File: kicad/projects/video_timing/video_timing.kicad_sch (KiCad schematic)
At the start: 26 parts, among them J1 peripheral_addr_bus_connector, J2 peripheral_aux_connector, J3 peripheral_membank_connector, U1 74HC161, U10 74HC30, U11 74HC30, U12 74HC30, U13 74HC30, U14 74HC30, U15 74HC30, U16 74HC30, U17 74HC30, U2 74HC161, U3 74HC161, U4 74HC161, U5 74HC161, U6 74HC04, U7 74HC04, U8 74HC00, U9 74HC00

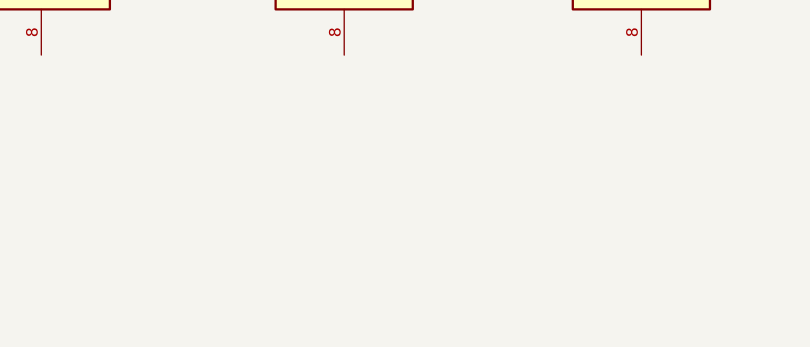
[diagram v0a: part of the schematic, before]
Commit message: Roughing out the video baords - time to switch to 157s for bank sel as well.
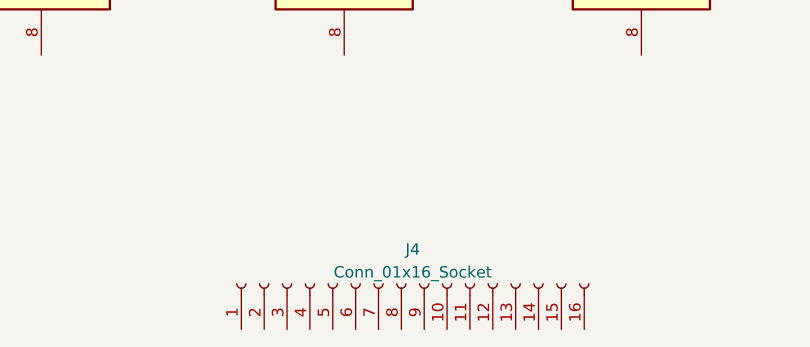
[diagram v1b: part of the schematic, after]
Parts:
- added J4: Conn_01x16_Socket, Connector_PinSocket_2.54mm:PinSocket_1x16_P2.54mm_Horizontal, symbol Connector:Conn_01x16_Socket
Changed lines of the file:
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@@
 (kicad_sch (version 20230121) (generator eeschema)
   (paper "B")
+  (bus_alias "BANK_BUS" (members "BANK_BUS_00" "BANK_BUS_01" "BANK_BUS_02" "BANK_BUS_03" "BANK_BUS_04" "BANK_BUS_05" "BANK_BUS_06" "BANK_BUS_07" "BANK_BUS_08" "BANK_BUS_09" "BANK_BUS_10" "BANK_BUS_11" "BANK_BUS_12" "BANK_BUS_13" "BANK_BUS_14" "BANK_BUS_15"))
+  (bus_alias "DATA_BUS" (members "DATA_BUS_00" "DATA_BUS_01" "DATA_BUS_02" "DATA_BUS_03" "DATA_BUS_04" "DATA_BUS_05" "DATA_BUS_06" "DATA_BUS_07" "DATA_BUS_08" "DATA_BUS_09" "DATA_BUS_10" "DATA_BUS_11" "DATA_BUS_12" "DATA_BUS_13" "DATA_BUS_14" "DATA_BUS_15"))
   (bus_alias "ADDR_BUS" (members "ADDR_BUS_00" "ADDR_BUS_01" "ADDR_BUS_02" "ADDR_BUS_03" "ADDR_BUS_04" "ADDR_BUS_05" "ADDR_BUS_06" "ADDR_BUS_07" "ADDR_BUS_08" "ADDR_BUS_09" "ADDR_BUS_10" "ADDR_BUS_11" "ADDR_BUS_12" "ADDR_BUS_13" "ADDR_BUS_14" "ADDR_BUS_15"))
-  (bus_alias "DATA_BUS" (members "DATA_BUS_00" "DATA_BUS_01" "DATA_BUS_02" "DATA_BUS_03" "DATA_BUS_04" "DATA_BUS_05" "DATA_BUS_06" "DATA_BUS_07" "DATA_BUS_08" "DATA_BUS_09" "DATA_BUS_10" "DATA_BUS_11" "DATA_BUS_12" "DATA_BUS_13" "DATA_BUS_14" "DATA_BUS_15"))
-  (bus_alias "BANK_BUS" (members "BANK_BUS_00" "BANK_BUS_01" "BANK_BUS_02" "BANK_BUS_03" "BANK_BUS_04" "BANK_BUS_05" "BANK_BUS_06" "BANK_BUS_07" "BANK_BUS_08" "BANK_BUS_09" "BANK_BUS_10" "BANK_BUS_11" "BANK_BUS_12" "BANK_BUS_13" "BANK_BUS_14" "BANK_BUS_15"))
   (junction (at 377.19 33.655) (diameter 0) (color 0 0 0 0)
   )
@@
         )
       )
+    )
+  )
+  (symbol (lib_id "Connector:Conn_01x16_Socket") (at 109.22 205.74 90) (unit 1)
+    (in_bom yes) (on_board yes) (dnp no) (fields_autoplaced)
+    (property "Reference" "J4" (at 110.49 201.93 90)
+      (effects (font (size 1.27 1.27)))
+    )
+    (property "Value" "Conn_01x16_Socket" (at 110.49 204.47 90)
+      (effects (font (size 1.27 1.27)))
+    )
+    (property "Footprint" "Connector_PinSocket_2.54mm:PinSocket_1x16_P2.54mm_Horizontal" (at 109.22 205.74 0)
+      (effects (font (size 1.27 1.27)) hide)
+    )
+    (property "Datasheet" "~" (at 109.22 205.74 0)
+      (effects (font (size 1.27 1.27)) hide)
+    )
+    (pin "1")
+    (pin "10")
+    (pin "11")
+    (pin "12")
+    (pin "13")
+    (pin "14")
+    (pin "15")
+    (pin "16")
+    (pin "2")
+    (pin "3")
+    (pin "4")
+    (pin "5")
+    (pin "6")
+    (pin "7")
+    (pin "8")
+    (pin "9")
+    (instances
+      (project "video_timing"
+        (path "/0c25b387-1696-4e3f-ab8e-df646088b074"
+          (reference "J4") (unit 1)
+        )
+      )

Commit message: Planning for video card.
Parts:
- added U18: 74HC161, Package_DIP:DIP-16_W7.62mm_Socket, symbol sixteen-bit-computer:74HC161
- added U19, U20: 74HC27, Package_DIP:DIP-14_W7.62mm_Socket, symbol sixteen-bit-computer:74HC27
- added X1: CXO_DIP8, Oscillator:Oscillator_DIP-8, symbol Oscillator:CXO_DIP8

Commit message: Schematic for video timing.
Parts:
- removed U20: 74HC27, Package_DIP:DIP-14_W7.62mm_Socket, symbol sixteen-bit-computer:74HC27
- added C10, C11, C12, C13, C14, C15, C16, C17, C18, C19, C2, C20, C21, C22, C3, C4, C5, C6, C7, C8, C9: C, Capacitor_THT:C_Disc_D5.0mm_W2.5mm_P5.00mm, symbol Device:C
- added U21: 74HC04, Package_DIP:DIP-14_W7.62mm_Socket, symbol 74xx:74HC04
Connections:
- net GND: now also U1.3 (P0), U1.4 (P1), U1.5 (P2), U1.6 (P3), U1.8 (GND), U10.7 (GND), U11.7 (GND), U12.7 (GND), U13.7 (GND), U14.7 (GND), U15.7 (GND), U16.7 (GND), U17.7 (GND), U18.3 (P0), U18.4 (P1), U18.5 (P2), U18.6 (P3), U18.8 (GND), U19.10, U19.11, U19.5, U19.7 (GND), U19.9, U2.3 (P0), U2.4 (P1), U2.5 (P2), U2.6 (P3), U2.8 (GND), U3.3 (P0), U3.4 (P1), U3.5 (P2), U3.6 (P3), U3.8 (GND), U4.3 (P0), U4.4 (P1), U4.5 (P2), U4.6 (P3), U4.8 (GND), U5.3 (P0), U5.4 (P1), U5.5 (P2), U5.6 (P3), U5.8 (GND), U6.7 (GND), U7.7 (GND), U8.7 (GND), U9.7 (GND), X1.4 (GND), C10.2, C11.2, C12.2, C13.2, C14.2, C15.2, C16.2, C17.2, C18.2, C19.2, C2.1, C20.2, C21.2, C22.2, C3.2, C4.1, C5.1, C6.1, C7.1, C8.1, C9.2, U21.11, U21.7 (GND), U21.9
- net VCC: now also U1.1 (~{MR}), U1.10 (TE), U1.16 (VCC), U1.7 (PE), U1.9 (~{SPE}), U10.14 (VCC), U11.14 (VCC), U12.14 (VCC), U13.14 (VCC), U14.14 (VCC), U15.14 (VCC), U16.14 (VCC), U17.14 (VCC), U18.1 (~{MR}), U18.10 (TE), U18.16 (VCC), U18.9 (~{SPE}), U19.14 (VCC), U2.1 (~{MR}), U2.10 (TE), U2.16 (VCC), U2.7 (PE), U2.9 (~{SPE}), U3.1 (~{MR}), U3.10 (TE), U3.16 (VCC), U3.9 (~{SPE}), U4.1 (~{MR}), U4.10 (TE), U4.16 (VCC), U4.7 (PE), U4.9 (~{SPE}), U5.1 (~{MR}), U5.10 (TE), U5.16 (VCC), U5.9 (~{SPE}), U6.14 (VCC), U7.14 (VCC), U8.14 (VCC), U9.14 (VCC), X1.8 (Vcc), C10.1, C11.1, C12.1, C13.1, C14.1, C15.1, C16.1, C17.1, C18.1, C19.1, C2.2, C20.1, C21.1, C22.1, C3.1, C4.2, C5.2, C6.2, C7.2, C8.2, C9.1, U21.14 (VCC)
- net COL_07: now reaches U3.11 (Q3)
- net COL_07: now also U12.12 (H), U13.12 (H), U7.3
- net COL_06: now reaches U3.12 (Q2)
- net COL_06: now also U12.11 (G), U13.11 (G), U7.1
- net COL_05: now reaches U3.13 (Q1)
- net COL_05: now also U11.6 (F), U6.13
- net COL_04: now reaches U3.14 (Q0)
- net COL_04: now also U10.5 (E), U6.11
- net at U3.2 (CP): now also U1.13 (Q1), U2.2 (CP)
- net at U3.7 (PE): now also U2.15 (TC)
- net ~{COL_05}: now reaches U6.12
- net ~{COL_05}: now also U10.6 (F), U12.6 (F), U13.6 (F)
- net ROW_00: now reaches U16.1 (A)
- net ROW_00: now also U15.1 (A), U17.1 (A), U4.14 (Q0), U7.5
- net ROW_09: now reaches U16.11 (G)
- net ROW_09: now also U17.11 (G), U18.13 (Q1), U21.5
- net ~{ROW_04_06_07}: now reaches U16.12 (H)
- net ~{ROW_04_06_07}: now also U14.12 (H), U15.12 (H), U17.12 (H), U19.12
- net ROW_01: now reaches U16.2 (B)
- net ROW_01: now also U14.2 (B), U15.2 (B), U4.13 (Q1), U7.9
- net ~{ROW_02}: now reaches U16.3 (C)
- net ~{ROW_02}: now also U14.3 (C), U15.3 (C), U7.10
- net ~{ROW_03}: now reaches U16.4 (D)
- net ~{ROW_03}: now also U14.4 (D), U15.4 (D), U7.12
- net ~{ROW_05}: now reaches U16.5 (E)
- net ~{ROW_05}: now also U14.5 (E), U17.5 (E), U21.2
- net ~{ROW_08}: now reaches U16.6 (F)
- net ~{ROW_08}: now also U14.6 (F), U15.6 (F), U17.6 (F), U21.4
- net ~{ROW_INDEX_515}: now reaches U16.8 (~{Y})
- net ~{ROW_INDEX_515}: now also U9.9
- net ~{ROW_00}: now reaches U14.1 (A)
- net ~{ROW_00}: now also U7.6
- net ~{ROW_09}: now reaches U14.11 (G)
- net ~{ROW_09}: now also U15.11 (G), U21.6
- net ~{ROW_INDEX_2}: now reaches U14.8 (~{Y})
- net ~{ROW_INDEX_2}: now also U9.1
- net at X1.5 (OUT): now also U1.2 (CP)
- net ~{COL_00}: now reaches U10.1 (A)
- net ~{COL_00}: now also U11.1 (A), U12.1 (A), U13.1 (A), U6.2
- net ~{COL_06}: now reaches U10.11 (G)
- net ~{COL_06}: now also U11.11 (G), U7.2
- net ~{COL_07}: now reaches U10.12 (H)
- net ~{COL_07}: now also U11.12 (H), U7.4
- net ~{COL_01}: now reaches U10.2 (B)
- net ~{COL_01}: now also U11.2 (B), U12.2 (B), U13.2 (B), U6.4
- net ~{COL_02}: now reaches U10.3 (C)
- net ~{COL_02}: now also U13.3 (C), U6.6
- net COL_03: now reaches U10.4 (D)
- net COL_03: now also U13.4 (D), U2.11 (Q3), U6.9
- net ~{COL_INDEX_24}: now reaches U10.8 (~{Y})
- net ~{COL_INDEX_24}: now also U8.1
- net ROW_03: now reaches U4.11 (Q3)
- net ROW_03: now also U17.4 (D), U7.13
- net ROW_02: now reaches U4.12 (Q2)
- net ROW_02: now also U17.3 (C), U7.11
- net at U4.15 (TC): now also U5.7 (PE)
- net ~{H_SYNC}: now reaches U4.2 (CP)
- net ~{H_SYNC}: now also U18.2 (CP), U5.2 (CP), U8.2, U8.6
- net H_BLANK: now reaches U19.3
- net H_BLANK: now also U8.12, U8.8
- net V_BLANK: now reaches U19.4
- net V_BLANK: now also U9.12, U9.8
- net ~{ANY_BLANK}: now reaches U19.6
- net ~{ANY_BLANK}: now also U21.13
- net ~{ROW_01}: now reaches U17.2 (B)
- net ~{ROW_01}: now also U7.8
- net ~{ROW_INDEX_525}: now reaches U17.8 (~{Y})
- net ~{ROW_INDEX_525}: now also U9.5
- net COL_00: now reaches U6.1
- net COL_00: now also U2.14 (Q0)
- net ROW_04: now reaches U19.1
- net ROW_04: now also U5.14 (Q0)
- net ROW_07: now reaches U19.13
- net ROW_07: now also U5.11 (Q3)
- net ROW_06: now reaches U19.2
- net ROW_06: now also U5.12 (Q2)
- net V_SYNC: now reaches U9.4
- net V_SYNC: now also U9.3
- net at U9.6: now also U9.2
- net COL_02: now reaches U2.12 (Q2)
- net COL_02: now also U11.3 (C), U12.3 (C), U6.5
- net COL_01: now reaches U2.13 (Q1)
- net COL_01: now also U6.3
- net at U8.11: now also U8.10
- net ~{COL_INDEX_36}: now reaches U8.13
- net ~{COL_INDEX_36}: now also U11.8 (~{Y})
- net at U9.10: now also U9.11
- net ROW_08: now reaches U18.14 (Q0)
- net ROW_08: now also U21.3
- net at U18.7 (PE): now also U5.15 (TC)
- net ~{COL_04}: now reaches U6.10
- net ~{COL_04}: now also U11.5 (E), U12.5 (E), U13.5 (E)
- net H_SYNC: now reaches U8.3
- net H_SYNC: now also U8.4
- net ~{COL_03}: now reaches U12.4 (D)
- net ~{COL_03}: now also U11.4 (D), U6.8
- net ~{COL_INDEX_196}: now reaches U12.8 (~{Y})
- net ~{COL_INDEX_196}: now also U8.9
- net ~{ROW_INDEX_35}: now reaches U9.13
- net ~{ROW_INDEX_35}: now also U15.8 (~{Y})
- net ROW_05: now reaches U5.13 (Q1)
- net ROW_05: now also U15.5 (E), U21.1
- net ~{COL_INDEX_200}: now reaches U13.8 (~{Y})
- net ~{COL_INDEX_200}: now also U8.5
- net ADDR_BUS_00: no longer names the net of J1.17 (A_00)
- net ADDR_BUS_01: no longer names the net of J1.18 (A_01)
- net ADDR_BUS_02: no longer names the net of J1.19 (A_02)
- net ADDR_BUS_03: no longer names the net of J1.20 (A_03)
- net ADDR_BUS_04: no longer names the net of J1.21 (A_04)
- net ADDR_BUS_05: no longer names the net of J1.22 (A_05)
- net ADDR_BUS_06: no longer names the net of J1.23 (A_06)
- net ADDR_BUS_07: no longer names the net of J1.24 (A_07)
- net ADDR_BUS_08: no longer names the net of J1.25 (A_08)
- net ADDR_BUS_09: no longer names the net of J1.26 (A_09)
- net ADDR_BUS_10: no longer names the net of J1.27 (A_10)
- net ADDR_BUS_11: no longer names the net of J1.28 (A_11)
- net ADDR_BUS_12: no longer names the net of J1.29 (A_12)
- net ADDR_BUS_13: no longer names the net of J1.30 (A_13)
- net ADDR_BUS_14: no longer names the net of J1.31 (A_14)
- net ADDR_BUS_15: no longer names the net of J1.32 (A_15)
- net BANK_BUS_00: no longer names the net of J3.1 (B_00)
- net BANK_BUS_01: no longer names the net of J3.2 (B_01)
- net BANK_BUS_02: no longer names the net of J3.3 (B_02)
- net BANK_BUS_03: no longer names the net of J3.4 (B_03)
- net BANK_BUS_04: no longer names the net of J3.5 (B_04)
- net BANK_BUS_05: no longer names the net of J3.6 (B_05)
- net BANK_BUS_06: no longer names the net of J3.7 (B_06)
- net BANK_BUS_07: no longer names the net of J3.8 (B_07)
- net BANK_BUS_08: no longer names the net of J3.9 (B_08)
- net BANK_BUS_09: no longer names the net of J3.10 (B_09)
- net BANK_BUS_10: no longer names the net of J3.11 (B_10)
- net BANK_BUS_11: no longer names the net of J3.12 (B_11)
- net BANK_BUS_12: no longer names the net of J3.13 (B_12)
- net BANK_BUS_13: no longer names the net of J3.14 (B_13)
- net BANK_BUS_14: no longer names the net of J3.15 (B_14)
- net BANK_BUS_15: no longer names the net of J3.16 (B_15)
- net DATA_BUS_00: no longer names the net of J1.1 (D_00)
- net DATA_BUS_01: no longer names the net of J1.2 (D_01)
- net DATA_BUS_02: no longer names the net of J1.3 (D_02)
- net DATA_BUS_03: no longer names the net of J1.4 (D_03)
- net DATA_BUS_04: no longer names the net of J1.5 (D_04)
- net DATA_BUS_05: no longer names the net of J1.6 (D_05)
- net DATA_BUS_06: no longer names the net of J1.7 (D_06)
- net DATA_BUS_07: no longer names the net of J1.8 (D_07)
- net DATA_BUS_08: no longer names the net of J1.9 (D_08)
- net DATA_BUS_09: no longer names the net of J1.10 (D_09)
- net DATA_BUS_10: no longer names the net of J1.11 (D_10)
- net DATA_BUS_11: no longer names the net of J1.12 (D_11)
- net DATA_BUS_12: no longer names the net of J1.13 (D_12)
- net DATA_BUS_13: no longer names the net of J1.14 (D_13)
- net DATA_BUS_14: no longer names the net of J1.15 (D_14)
- net DATA_BUS_15: no longer names the net of J1.16 (D_15)
- new net ANY_BLANK: U21.12
- no-connect marks 0 -> 65
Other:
- note added: "Clock Division"
- note added: "Column count"
- note added: "Coulmn inverts"
- note added: "HSync and HBlank gen"
- note added: "Q"
- note added: "Row count"
- note added: "Row inverts"
- note added: "SR Latch"
- note added: "VSync and VBlank gen"
- note added: "~{Q}"
- note added: "~{R}"
- note added: "~{S}"
- moved on the sheet: C1, C97, C98, C99, J1, J2, J3, J4, R1, TP1, U1, U10A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

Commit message: Start laying out video timing.
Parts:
- removed U19: 74HC27, Package_DIP:DIP-14_W7.62mm_Socket, symbol sixteen-bit-computer:74HC27
- added U20: 74HC11, Package_DIP:DIP-14_W7.62mm_Socket, symbol sixteen-bit-computer:74HC11
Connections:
- net ANY_BLANK is gone; now on net ~{ROW_09}: U21.12
- net ~{ANY_BLANK} is gone; now on net ROW_09: U21.13
- net COL_00: now also J4.9 (Pin_9), U21.3; no longer U6.1
- net COL_01: now also J4.10 (Pin_10)
- net COL_02: now also J4.11 (Pin_11)
- net COL_03: now also J4.12 (Pin_12), U12.4 (D); no longer U10.4 (D)
- net COL_04: now also J4.13 (Pin_13), U12.5 (E); no longer U10.5 (E)
- net COL_05: now also J4.14 (Pin_14), U10.6 (F), U12.6 (F)
- net COL_06: now also J4.15 (Pin_15), U21.1; no longer U12.11 (G), U7.1
- net COL_07: now also J4.16 (Pin_16), U10.12 (H), U11.12 (H); no longer U7.3
- net GND: now also U21.5, U20.1, U20.10, U20.11, U20.13, U20.2, U20.7 (GND), U20.9
- net ROW_00: now also U7.3; no longer U15.1 (A), U16.1 (A), U7.5
- net ROW_01: now also U7.5; no longer U14.2 (B), U16.2 (B), U7.9
- net ROW_02: now also J4.1 (Pin_1), U16.3 (C), U7.9; no longer U7.11
- net ROW_03: now also J4.2 (Pin_2), U15.4 (D), U16.4 (D), U7.11; no longer U7.13
- net ROW_04: now also J4.3 (Pin_3), U7.13
- net ROW_05: now also J4.4 (Pin_4), U20.3; no longer U15.5 (E), U21.1
- net ROW_06: now also J4.5 (Pin_5), U20.4
- net ROW_07: now also J4.6 (Pin_6), U20.5
- net ROW_08: now also J4.7 (Pin_7), U14.6 (F), U15.6 (F), U16.6 (F), U7.1; no longer U21.3
- net ROW_09: now also J4.8 (Pin_8); no longer U16.11 (G), U21.5
- net VCC: now also U17.12 (H), U20.14 (VCC); no longer U18.1 (~{MR}), U2.1 (~{MR}), U3.1 (~{MR}), U4.1 (~{MR}), U5.1 (~{MR})
- net ~{COL_00}: now also U21.4; no longer U6.2
- net ~{COL_03}: now also U10.4 (D); no longer U12.4 (D)
- net ~{COL_04}: now also U10.5 (E); no longer U12.5 (E)
- net ~{COL_05}: no longer U10.6 (F), U12.6 (F)
- net ~{COL_06}: now also U12.11 (G), U21.2; no longer U7.2
- net ~{COL_INDEX_200}: now also U2.1 (~{MR}), U3.1 (~{MR}), U8.13; no longer U8.5
- net ~{ROW_00}: now also U15.1 (A), U16.1 (A), U7.4; no longer U7.6
- net ~{ROW_01}: now also U14.2 (B), U16.2 (B), U7.6; no longer U7.8
- net ~{ROW_02}: now also U7.8; no longer U16.3 (C), U7.10
- net ~{ROW_03}: now also U7.10; no longer U15.4 (D), U16.4 (D), U7.12
- net ~{ROW_08}: now also U7.2; no longer U14.6 (F), U15.6 (F), U16.6 (F), U21.4
- net ~{ROW_09}: now also U16.11 (G); no longer U21.6
- net ~{ROW_INDEX_525}: now also U18.1 (~{MR}), U4.1 (~{MR}), U5.1 (~{MR}), U9.13; no longer U9.5
- net PIXEL_CLOCK: now reaches U1.13 (Q1), U2.2 (CP), U3.2 (CP)
- net PIXEL_CLOCK: now also U6.1
- removed net ~{COL_07}: U10.12 (H), U11.12 (H), U7.4
- net ~{COL_INDEX_196} renamed ~{COL_INDEX_160}
- net ~{COL_INDEX_160}: now also U10.8 (~{Y}); no longer U12.8 (~{Y})
- net ~{COL_INDEX_24} renamed ~{COL_INDEX_188}
- net ~{COL_INDEX_188}: now also U12.8 (~{Y}); no longer U10.8 (~{Y})
- net ~{COL_INDEX_36} renamed ~{COL_INDEX_164}
- net ~{COL_INDEX_164}: now also U8.5; no longer U8.13
- net ~{ROW_04_06_07} renamed ROW_05_06_07
- net ROW_05_06_07: now also U20.6; no longer U17.12 (H)
- net ~{ROW_05} renamed ~{ROW_04}
- net ~{ROW_04}: now also U15.5 (E), U7.12; no longer U21.2
- net ~{ROW_INDEX_2} renamed ~{ROW_INDEX_480}
- net ~{ROW_INDEX_480}: now also U9.9; no longer U9.1
- net ~{ROW_INDEX_35} renamed ~{ROW_INDEX_490}
- net ~{ROW_INDEX_490}: now also U9.5; no longer U9.13
- net ~{ROW_INDEX_515} renamed ~{ROW_INDEX_492}
- net ~{ROW_INDEX_492}: now also U9.1; no longer U9.9
- new net ~{PIXEL_CLOCK}: U6.2
- no-connect marks 65 -> 68
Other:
- note added: "SR Latch Blank"
- note added: "SR Latch Sync"
- note removed: "SR Latch"
- moved on the sheet: C2, C3, C4, C5, C6, C7, C8, J4, U1, U10A, U11A, U12A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

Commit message: Add music planning and some extra work planning video card layouts.
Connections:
- no-connect marks 68 -> 67
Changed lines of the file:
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@@
 (kicad_sch (version 20230121) (generator eeschema)
   (paper "C")
+  (bus_alias "BANK_BUS" (members "BANK_BUS_00" "BANK_BUS_01" "BANK_BUS_02" "BANK_BUS_03" "BANK_BUS_04" "BANK_BUS_05" "BANK_BUS_06" "BANK_BUS_07" "BANK_BUS_08" "BANK_BUS_09" "BANK_BUS_10" "BANK_BUS_11" "BANK_BUS_12" "BANK_BUS_13" "BANK_BUS_14" "BANK_BUS_15"))
   (bus_alias "ROW_BUS" (members "ROW_00" "ROW_01" "ROW_02" "ROW_03" "ROW_04" "ROW_05" "ROW_06" "ROW_07" "ROW_08" "ROW_09" "~{ROW_00}" "~{ROW_01}" "~{ROW_02}" "~{ROW_03}" "~{ROW_05}" "~{ROW_08}" "~{ROW_09}" "ROW_05_06_07" "~{ROW_04}"))
   (bus_alias "ADDR_BUS" (members "ADDR_BUS_00" "ADDR_BUS_01" "ADDR_BUS_02" "ADDR_BUS_03" "ADDR_BUS_04" "ADDR_BUS_05" "ADDR_BUS_06" "ADDR_BUS_07" "ADDR_BUS_08" "ADDR_BUS_09" "ADDR_BUS_10" "ADDR_BUS_11" "ADDR_BUS_12" "ADDR_BUS_13" "ADDR_BUS_14" "ADDR_BUS_15"))
   (bus_alias "COL_BUS" (members "COL_00" "COL_01" "COL_02" "COL_03" "COL_04" "COL_05" "COL_06" "COL_07" "~{COL_00}" "~{COL_01}" "~{COL_02}" "~{COL_03}" "~{COL_04}" "~{COL_05}" "~{COL_06}" "~{COL_07}"))
   (bus_alias "DATA_BUS" (members "DATA_BUS_00" "DATA_BUS_01" "DATA_BUS_02" "DATA_BUS_03" "DATA_BUS_04" "DATA_BUS_05" "DATA_BUS_06" "DATA_BUS_07" "DATA_BUS_08" "DATA_BUS_09" "DATA_BUS_10" "DATA_BUS_11" "DATA_BUS_12" "DATA_BUS_13" "DATA_BUS_14" "DATA_BUS_15"))
-  (bus_alias "BANK_BUS" (members "BANK_BUS_00" "BANK_BUS_01" "BANK_BUS_02" "BANK_BUS_03" "BANK_BUS_04" "BANK_BUS_05" "BANK_BUS_06" "BANK_BUS_07" "BANK_BUS_08" "BANK_BUS_09" "BANK_BUS_10" "BANK_BUS_11" "BANK_BUS_12" "BANK_BUS_13" "BANK_BUS_14" "BANK_BUS_15"))
   (junction (at 156.845 300.355) (diameter 0) (color 0 0 0 0)
   )
@@
   (no_connect (at 443.865 52.07))
   (no_connect (at 401.32 35.56))
-  (no_connect (at 414.02 167.005))
   (no_connect (at 401.32 83.82))
   (no_connect (at 443.865 41.91))
